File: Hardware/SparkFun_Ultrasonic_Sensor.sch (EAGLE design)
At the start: 64 parts, among them J4 Vertical Qwiic Connector, J6 Vertical Qwiic Connector, Q1 600mA/40V, U5 ULTRASONIC_SENSOR_TRANSMITTER, U6 LMV324, U7 STM8L051F3, U8 SP3232EB, U9 ULTRASONIC_SENSOR_RECEIVER

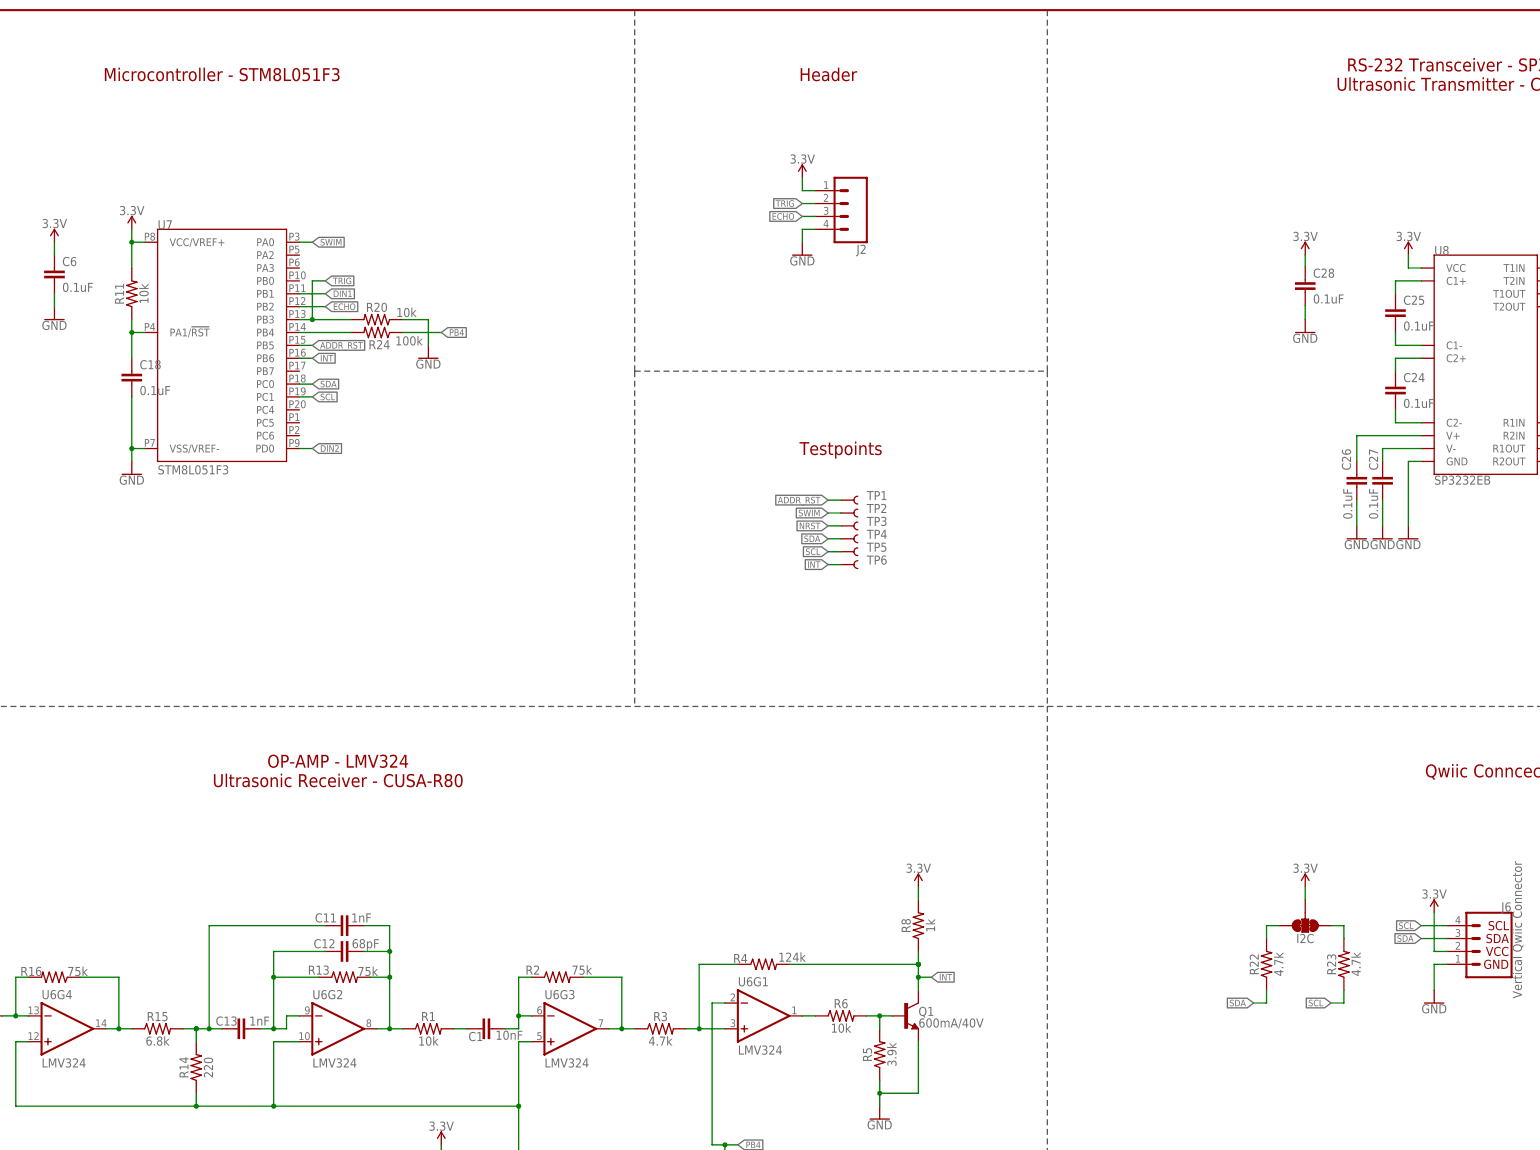
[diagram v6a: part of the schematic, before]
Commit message: Fixes various schematic elements, some acid traps, and improves ground pour
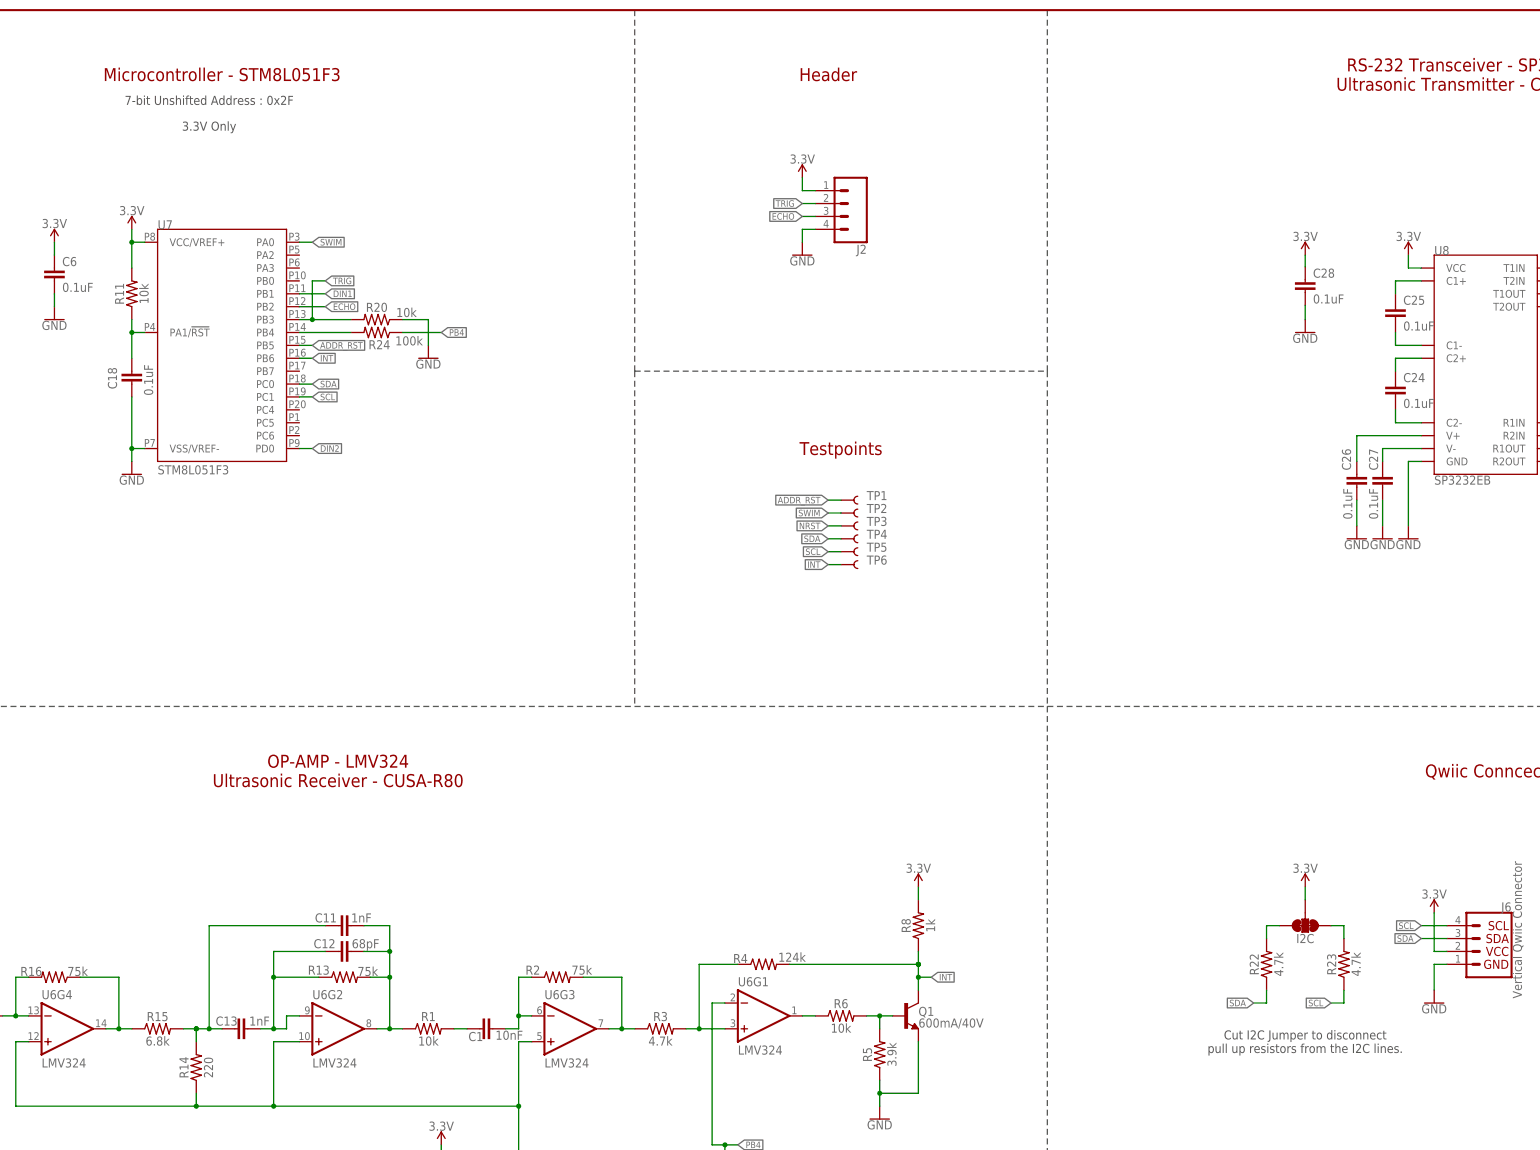
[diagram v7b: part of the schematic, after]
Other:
- note added: "3.3V Only"
- note added: "7-bit Unshifted Address : 0x2F"
- note added: "Cut I2C Jumper to disconnect pull up resistors from the I2C lines."
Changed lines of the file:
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@@
 <wire x1="177.8" y1="208.28" x2="177.8" y2="142.24" width="0.254" layer="97" style="longdash"/>
 <wire x1="177.8" y1="208.28" x2="259.08" y2="208.28" width="0.254" layer="97" style="longdash"/>
+<text x="309.88" y="76.2" size="1.778" layer="97" font="vector" align="center">Cut I2C Jumper to disconnect
+pull up resistors from the I2C lines.</text>
+<text x="93.98" y="261.62" size="1.778" layer="97" font="vector" align="center">7-bit Unshifted Address : 0x2F</text>
+<text x="93.98" y="256.54" size="1.778" layer="97" font="vector" align="center">3.3V Only</text>
 </plain>
 <instances>
@@
 </instance>
 <instance part="C18" gate="G$1" x="78.74" y="205.74" smashed="yes">
-<attribute name="NAME" x="80.264" y="208.661" size="1.778" layer="95" font="vector"/>
-<attribute name="VALUE" x="80.264" y="203.581" size="1.778" layer="96" font="vector"/>
+<attribute name="NAME" x="75.819" y="204.724" size="1.778" layer="95" font="vector" rot="R90"/>
+<attribute name="VALUE" x="82.931" y="203.454" size="1.778" layer="96" font="vector" rot="R90"/>
 </instance>
 <instance part="R11" gate="G$1" x="78.74" y="223.52" smashed="yes" rot="R90">

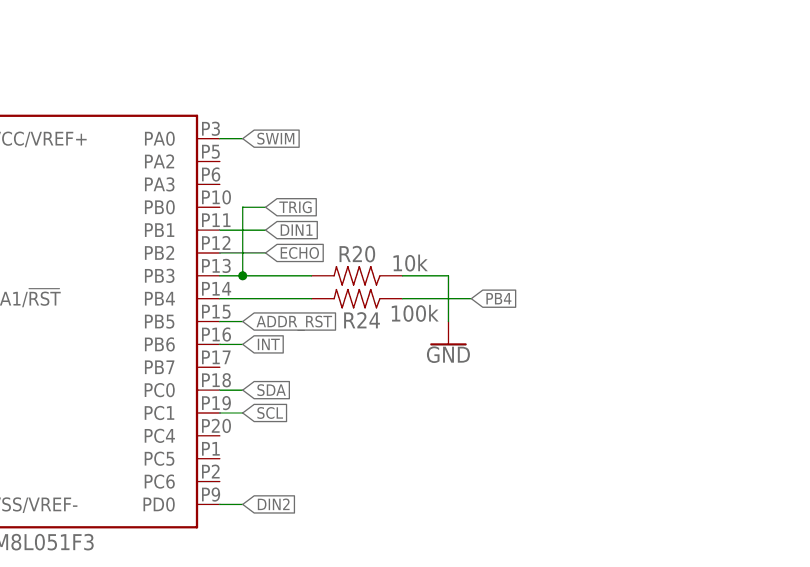
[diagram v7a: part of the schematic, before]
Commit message: Moves some more parts away from the sensor through holes and updates the schematic
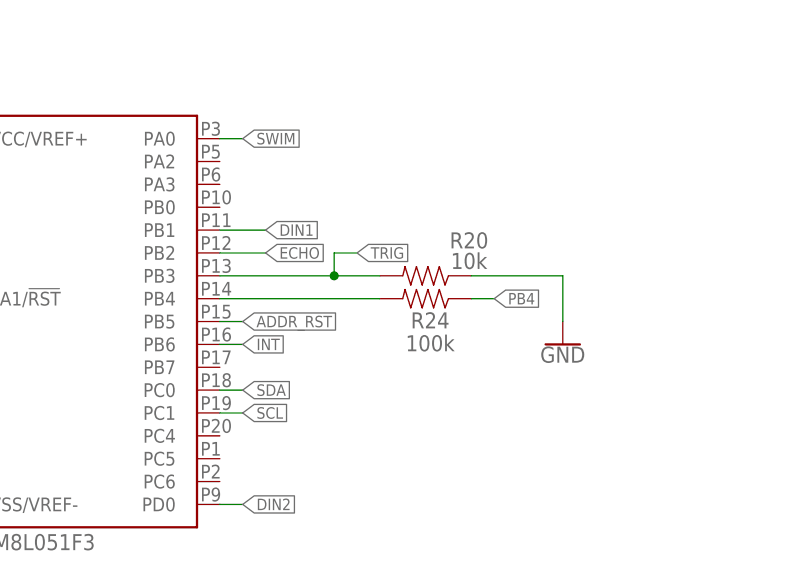
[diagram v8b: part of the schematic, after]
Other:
- moved on the sheet: R20, R24
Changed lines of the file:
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@@
 <attribute name="VALUE" x="80.264" y="223.52" size="1.778" layer="96" font="vector" rot="R90" align="top-center"/>
 </instance>
-<instance part="R20" gate="G$1" x="127" y="218.44" smashed="yes" rot="R180">
-<attribute name="NAME" x="127" y="221.742" size="1.778" layer="95" font="vector" rot="R180" align="bottom-center"/>
-<attribute name="VALUE" x="132.842" y="218.948" size="1.778" layer="96" font="vector" rot="R180" align="top-center"/>
-</instance>
-<instance part="R24" gate="G$1" x="127" y="215.9" smashed="yes" rot="R180">
-<attribute name="NAME" x="127.508" y="214.376" size="1.778" layer="95" font="vector" rot="R180" align="bottom-center"/>
-<attribute name="VALUE" x="133.35" y="213.36" size="1.778" layer="96" font="vector" rot="R180" align="top-center"/>
+<instance part="R20" gate="G$1" x="134.62" y="218.44" smashed="yes" rot="R180">
+<attribute name="NAME" x="139.446" y="223.266" size="1.778" layer="95" font="vector" rot="R180" align="bottom-center"/>
+<attribute name="VALUE" x="139.446" y="219.202" size="1.778" layer="96" font="vector" rot="R180" align="top-center"/>
+</instance>
+<instance part="R24" gate="G$1" x="134.62" y="215.9" smashed="yes" rot="R180">
+<attribute name="NAME" x="135.128" y="214.376" size="1.778" layer="95" font="vector" rot="R180" align="bottom-center"/>
+<attribute name="VALUE" x="135.128" y="210.058" size="1.778" layer="96" font="vector" rot="R180" align="top-center"/>
 </instance>
 <instance part="SUPPLY1" gate="G$1" x="78.74" y="236.22" smashed="yes">
@@
 <attribute name="VALUE" x="63.5" y="218.186" size="1.778" layer="96" font="vector" align="top-center"/>
 </instance>
-<instance part="GND18" gate="1" x="137.16" y="210.82" smashed="yes">
-<attribute name="VALUE" x="137.16" y="210.566" size="1.778" layer="96" font="vector" align="top-center"/>
+<instance part="GND18" gate="1" x="149.86" y="210.82" smashed="yes">
+<attribute name="VALUE" x="149.86" y="210.566" size="1.778" layer="96" font="vector" align="top-center"/>
 </instance>
 <instance part="TP1" gate="G$1" x="218.44" y="182.88" smashed="yes">
@@
 <segment>
 <pinref part="R20" gate="G$1" pin="1"/>
-<wire x1="132.08" y1="218.44" x2="137.16" y2="218.44" width="0.1524" layer="91"/>
-<wire x1="137.16" y1="218.44" x2="137.16" y2="213.36" width="0.1524" layer="91"/>
+<wire x1="139.7" y1="218.44" x2="149.86" y2="218.44" width="0.1524" layer="91"/>
+<wire x1="149.86" y1="218.44" x2="149.86" y2="213.36" width="0.1524" layer="91"/>
 <pinref part="GND18" gate="1" pin="GND"/>
 </segment>
@@
 <pinref part="U7" gate="G$1" pin="PB3"/>
 <pinref part="R20" gate="G$1" pin="2"/>
-<wire x1="111.76" y1="218.44" x2="114.3" y2="218.44" width="0.1524" layer="91"/>
-<wire x1="114.3" y1="218.44" x2="121.92" y2="218.44" width="0.1524" layer="91"/>
-<wire x1="114.3" y1="226.06" x2="114.3" y2="218.44" width="0.1524" layer="91"/>
-<junction x="114.3" y="218.44"/>
-<wire x1="114.3" y1="226.06" x2="116.84" y2="226.06" width="0.1524" layer="91"/>
-<label x="116.84" y="226.06" size="1.27" layer="95" font="vector" xref="yes"/>
+<wire x1="111.76" y1="218.44" x2="124.46" y2="218.44" width="0.1524" layer="91"/>
+<wire x1="124.46" y1="218.44" x2="129.54" y2="218.44" width="0.1524" layer="91"/>
+<wire x1="124.46" y1="220.98" x2="124.46" y2="218.44" width="0.1524" layer="91"/>
+<junction x="124.46" y="218.44"/>
+<wire x1="124.46" y1="220.98" x2="127" y2="220.98" width="0.1524" layer="91"/>
+<label x="127" y="220.98" size="1.27" layer="95" font="vector" xref="yes"/>
 </segment>
 <segment>
@@
 <segment>
 <pinref part="R24" gate="G$1" pin="1"/>
-<wire x1="132.08" y1="215.9" x2="139.7" y2="215.9" width="0.1524" layer="91"/>
-<label x="139.7" y="215.9" size="1.27" layer="95" font="vector" xref="yes"/>
+<wire x1="139.7" y1="215.9" x2="142.24" y2="215.9" width="0.1524" layer="91"/>
+<label x="142.24" y="215.9" size="1.27" layer="95" font="vector" xref="yes"/>
 </segment>
 </net>
@@
 <pinref part="U7" gate="G$1" pin="PB4"/>
 <pinref part="R24" gate="G$1" pin="2"/>
-<wire x1="121.92" y1="215.9" x2="111.76" y2="215.9" width="0.1524" layer="91"/>
-</segment>
-</net>
+<wire x1="129.54" y1="215.9" x2="111.76" y2="215.9" width="0.1524" layer="91"/>
+</segment>
+</net>
